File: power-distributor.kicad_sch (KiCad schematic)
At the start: 9 parts, among them J11 Barrel_Jack, J21 Barrel_Jack, J22 Barrel_Jack, J23 Barrel_Jack, J24 Barrel_Jack, J25 Barrel_Jack

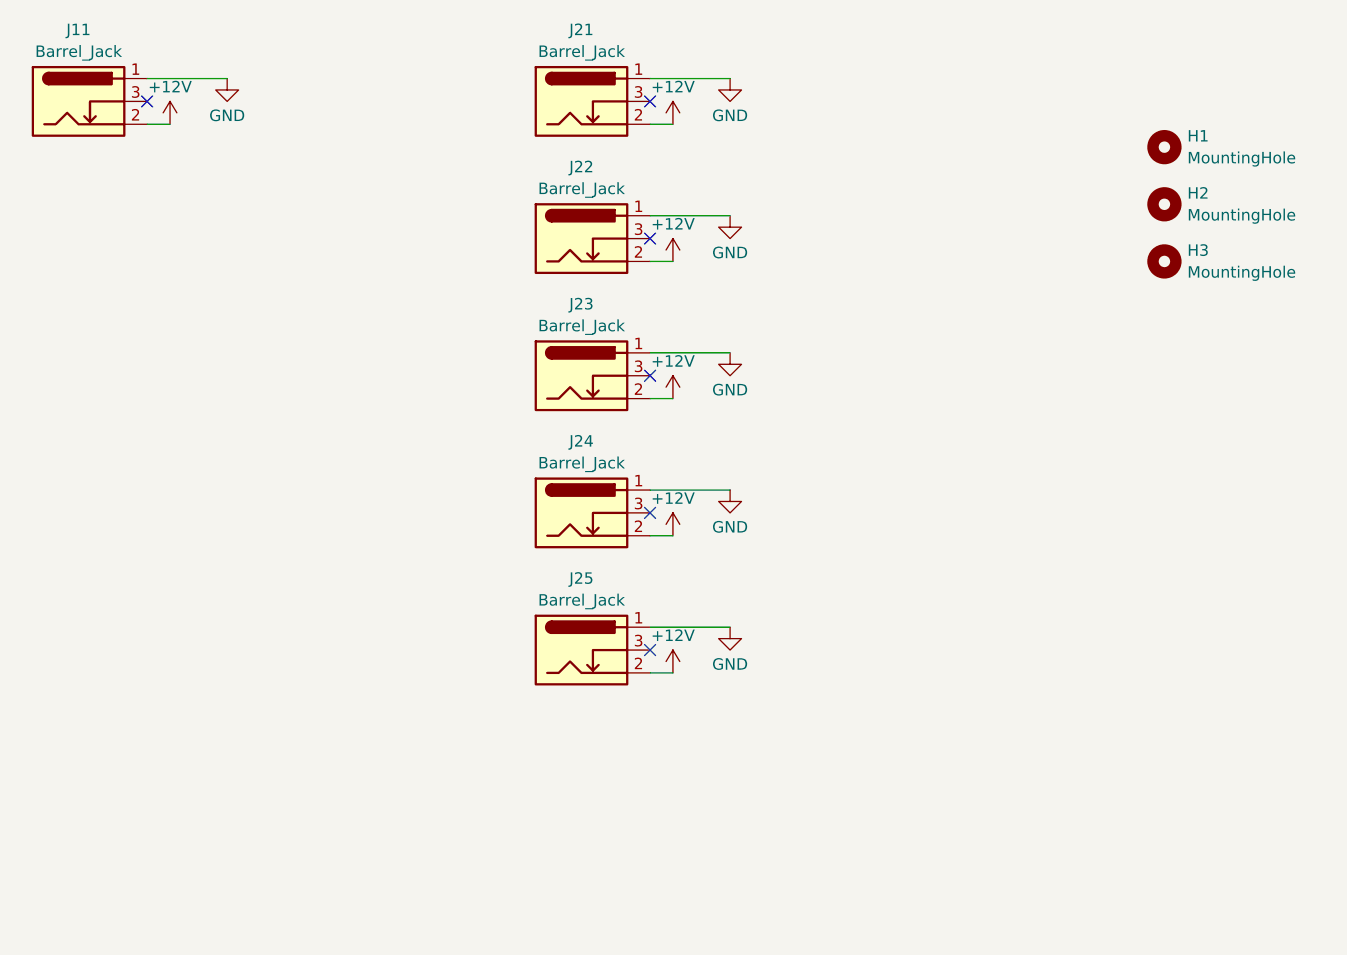
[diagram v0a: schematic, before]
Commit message: v02: Bigger mounting holes, more even spacing
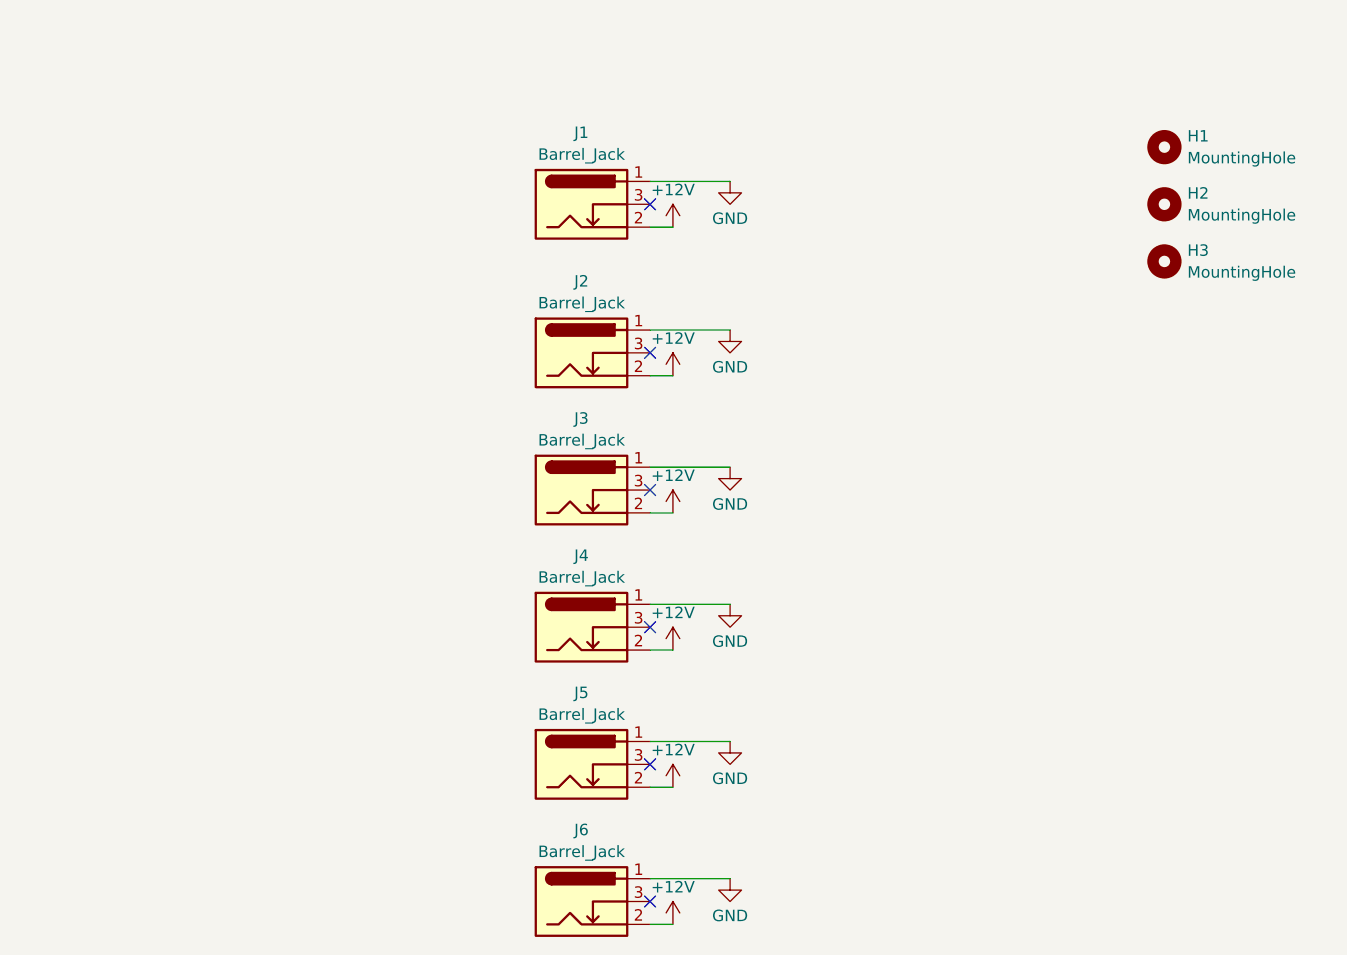
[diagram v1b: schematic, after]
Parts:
- renumbered J11 to J1, J21 to J2, J22 to J3, J23 to J4, J24 to J5, J25 to J6
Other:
- moved on the sheet: J1, J2, J3, J4, J5, J6
